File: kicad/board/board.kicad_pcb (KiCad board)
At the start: 2 copper layers, 126.9 x 103.7 mm, 43 parts

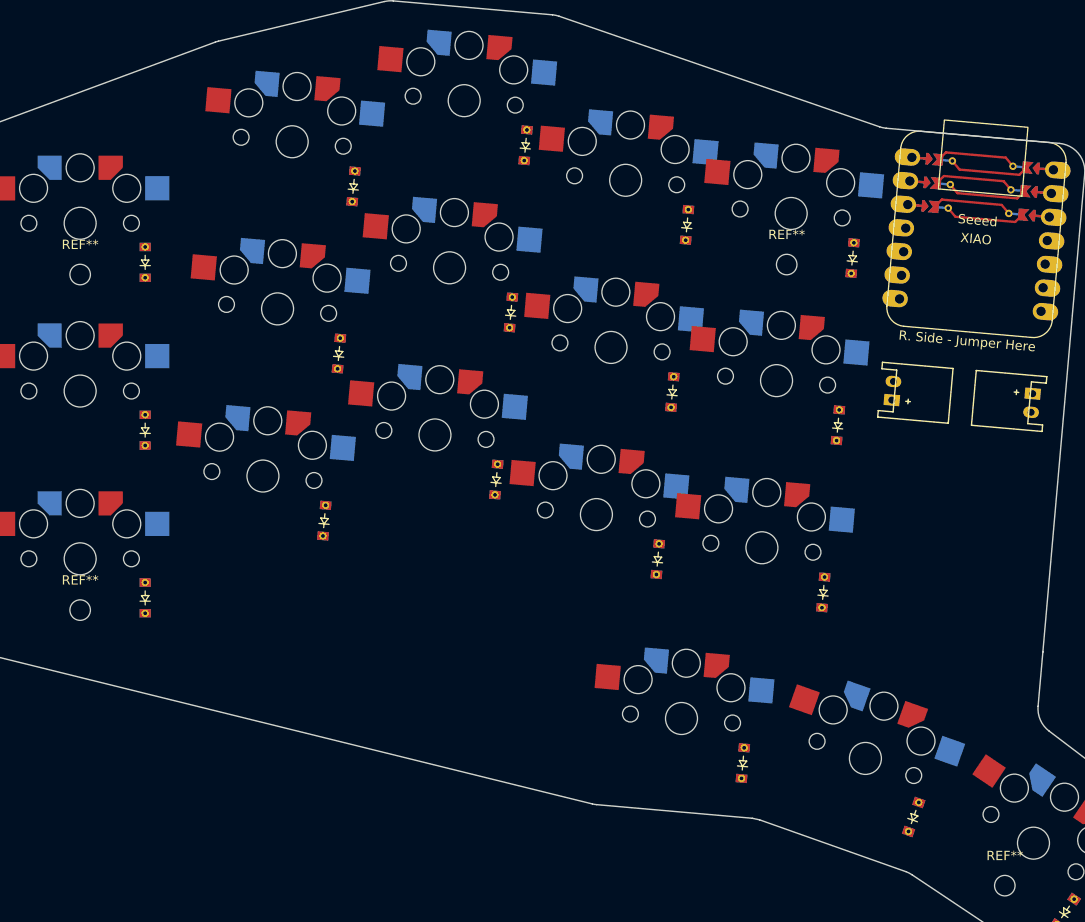
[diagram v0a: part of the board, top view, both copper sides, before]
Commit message: added diodes
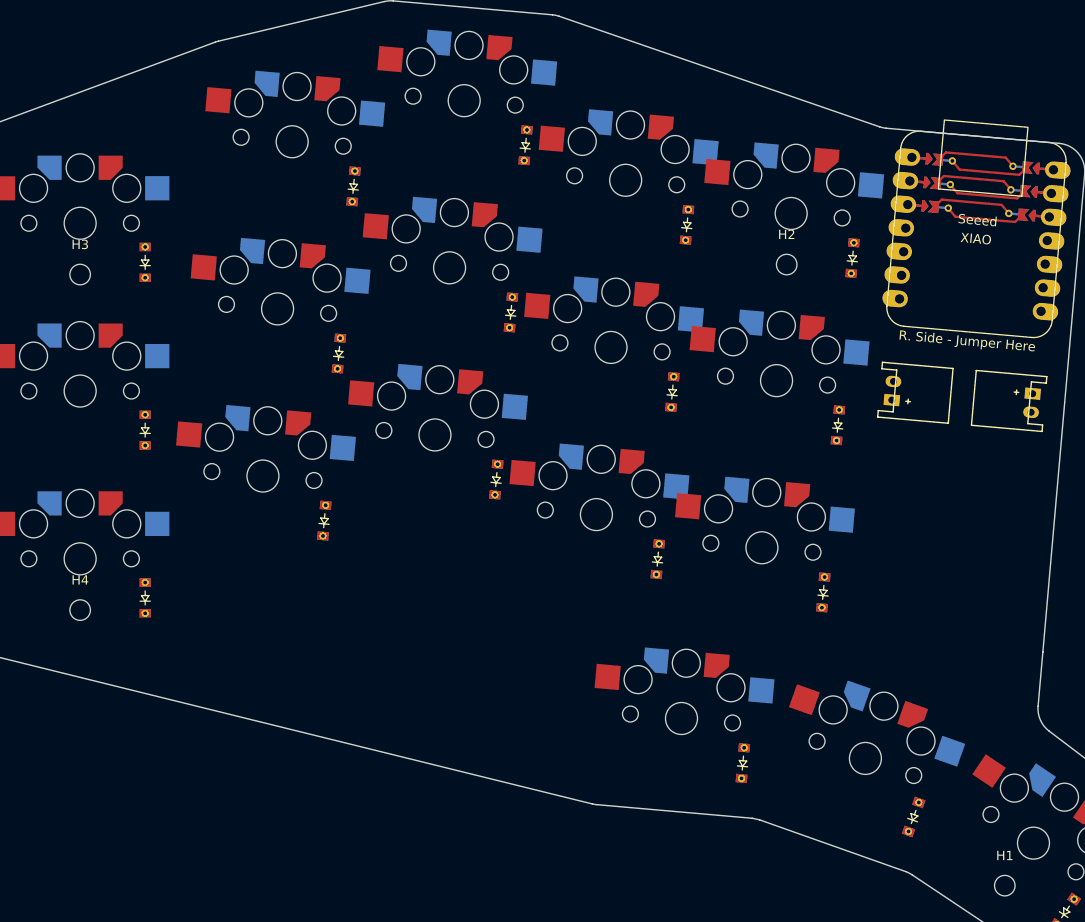
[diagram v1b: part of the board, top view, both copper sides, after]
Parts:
- renumbered REF** to H1, REF** to H2, REF** to H3, REF** to H4
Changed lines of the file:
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@@
 		)
 		(pad "" np_thru_hole circle
-			(at 5.000001 -3.75 355)
+			(at 5.000002 -3.75 355)
 			(size 3 3)
 			(drill 3)
@@
 		)
 		(pad "" np_thru_hole circle
-			(at 5.000001 -3.75 355)
+			(at 5.000002 -3.75 355)
 			(size 3 3)
 			(drill 3)
@@
 		(descr "Mounting Hole 2.2mm, no annular, M2")
 		(tags "mounting hole 2.2mm no annular m2")
-		(property "Reference" "REF**"
+		(property "Reference" "H3"
 			(at 0 -3.2 0)
 			(layer "F.SilkS")
@@
 		)
 		(pad "" np_thru_hole circle
-			(at 5.000001 -3.75 355)
+			(at 5.000002 -3.75 355)
 			(size 3 3)
 			(drill 3)
@@
 		)
 		(pad "" np_thru_hole circle
-			(at 5.000001 -3.75 355)
+			(at 5.000002 -3.75 355)
 			(size 3 3)
 			(drill 3)
@@
 		)
 		(pad "" np_thru_hole circle
-			(at 5.000001 -3.75 355)
+			(at 5.000002 -3.75 355)
 			(size 3 3)
 			(drill 3)
@@
 		)
 		(pad "" np_thru_hole circle
-			(at 5.000001 -3.75 355)
+			(at 5.000002 -3.75 355)
 			(size 3 3)
 			(drill 3)
@@
 		(at 19.610296 -8.88183 -5)
 		(property "Reference" "S4"
-			(at 0 0 -5)
+			(at 0 0 175)
 			(layer "F.SilkS")
 			(hide yes)
@@
 		)
 		(property "Value" "SW_Push_45deg"
-			(at 0 0 -5)
+			(at 0 0 175)
 			(layer "F.SilkS")
 			(hide yes)
@@
 		)
 		(property "Footprint" ""
-			(at 0 0 -5)
+			(at 0 0 175)
 			(layer "F.Fab")
 			(hide yes)
@@
 		)
 		(property "Datasheet" ""
-			(at 0 0 -5)
+			(at 0 0 175)
 			(layer "F.Fab")
 			(hide yes)
@@
 		)
 		(property "Description" "Push button switch, normally open, two pins, 45° tilted"
-			(at 0 0 -5)
+			(at 0 0 175)
 			(layer "F.Fab")
 			(hide yes)
@@
 		)
 		(pad "" np_thru_hole circle
-			(at 5.000001 -3.75 355)
+			(at 5.000002 -3.75 355)
 			(size 3 3)
 			(drill 3)
@@
 		)
 		(pad "" np_thru_hole circle
-			(at 5.000001 -3.75 355)
+			(at 5.000002 -3.75 355)
 			(size 3 3)
 			(drill 3)
@@
 		(descr "Mounting Hole 2.2mm, no annular, M2")
 		(tags "mounting hole 2.2mm no annular m2")
-		(property "Reference" "REF**"
+		(property "Reference" "H1"
 			(at 0 -3.2 0)
 			(layer "F.SilkS")
@@
 			(size 2.2 2.2)
 			(drill 2.2)
-			(layers "*.Cu" "*.Mask")
+			(layers "F&B.Cu" "*.Mask")
 		)
 	)
@@
 		)
 		(pad "" np_thru_hole circle
-			(at 5.000001 -3.75 355)
+			(at 5.000002 -3.75 355)
 			(size 3 3)
 			(drill 3)
@@
 		)
 		(property "Footprint" ""
-			(at 0 0 -5)
+			(at 0 0 175)
 			(layer "F.Fab")
 			(hide yes)
@@
 		)
 		(property "Datasheet" ""
-			(at 0 0 -5)
+			(at 0 0 175)
 			(layer "F.Fab")
 			(hide yes)
@@
 		)
 		(property "Description" ""
-			(at 0 0 -5)
+			(at 0 0 175)
 			(layer "F.Fab")
 			(hide yes)
@@
 		)
 		(pad "1" smd custom
-			(at -4.775001 -5.08 355)
+			(at -4.775002 -5.08 355)
 			(size 0.2 0.2)
 			(layers "B.Cu" "B.Mask")
@@
 		)
 		(pad "2" thru_hole circle
-			(at -3.262001 -2.54)
+			(at -3.262002 -2.54)
 			(size 0.8 0.8)
 			(drill 0.4)
@@
 		)
 		(pad "12" smd custom
-			(at -4.775001 -5.08 355)
+			(at -4.775002 -5.08 355)
 			(size 0.2 0.2)
 			(layers "F.Cu" "F.Mask")
@@
 		(descr "Mounting Hole 2.2mm, no annular, M2")
 		(tags "mounting hole 2.2mm no annular m2")
-		(property "Reference" "REF**"
+		(property "Reference" "H2"
 			(at 0 -3.2 0)
 			(layer "F.SilkS")
@@
 		)
 		(pad "" np_thru_hole circle
-			(at 5.000001 -3.75 355)
+			(at 5.000002 -3.75 355)
 			(size 3 3)
 			(drill 3)
@@
 		(descr "Mounting Hole 2.2mm, no annular, M2")
 		(tags "mounting hole 2.2mm no annular m2")
-		(property "Reference" "REF**"
+		(property "Reference" "H4"
 			(at 0 -3.2 0)
 			(layer "F.SilkS")
@@
 		)
 		(pad "" np_thru_hole circle
-			(at 5.000001 -3.75 355)
+			(at 5.000002 -3.75 355)
 			(size 3 3)
 			(drill 3)
@@
 		)
 		(pad "" np_thru_hole circle
-			(at 5.000001 -3.75 355)
+			(at 5.000002 -3.75 355)
 			(size 3 3)
 			(drill 3)
@@
 		)
 		(pad "" np_thru_hole circle
-			(at 5.000001 -3.75 355)
+			(at 5.000002 -3.75 355)
 			(size 3 3)
 			(drill 3)

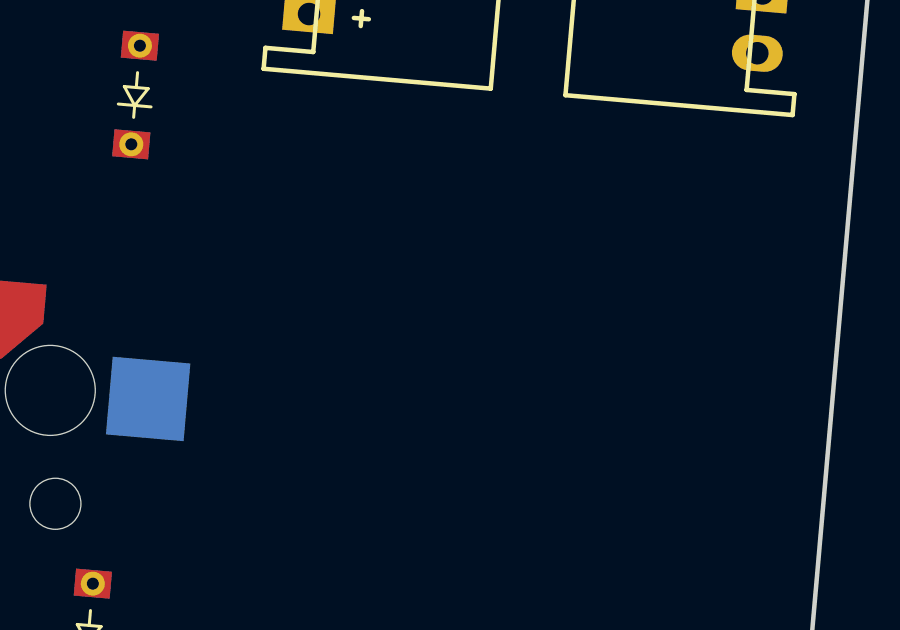
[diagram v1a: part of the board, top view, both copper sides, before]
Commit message: fixed footprints
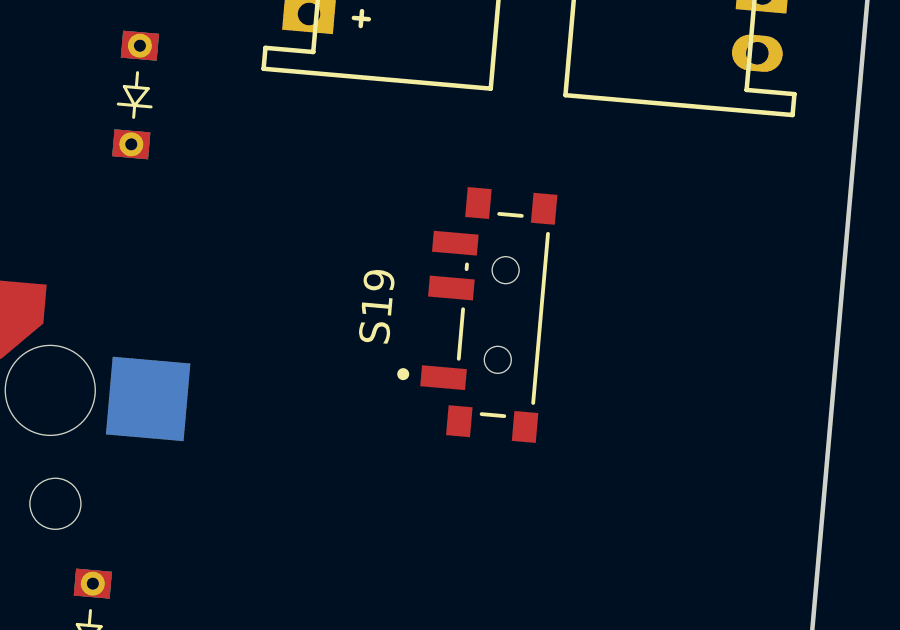
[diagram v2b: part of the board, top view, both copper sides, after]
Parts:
- added S19: SW_SSSS811101, sCLACKEN:SW_SSSS811101, F.Cu at (93.5, -7.00)

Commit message: we messed up pcb
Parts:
- added S20: SSSS811101, sCLACKEN:SW_SSSS811101, B.Cu at (255.0, 154.5)
- D1, D10, D11, D12, D13, D14, D15, D16, D17, D18, D2, D3, D4, D5, D6, D7, D8, D9: value 1N914 -> D
- H1, H2, H3, H4: value MountingHole_2.2mm_M2 -> MountingHole
- S1, S10, S11, S12, S13, S14, S15, S16, S17, S18, S2, S3, S4, S5, S6, S7, S8, S9: value SW_Push_45deg -> SW_SPST
- S19: value SW_SSSS811101 -> SSSS811101
- U1: value (none) -> ~; footprint xiao-ble-tht -> clacken:seeed_xaio
- moved S19 228.4 mm to (255.0, 154.5)
- moved D11 220.4 mm to (216.0, 141.2)
- moved D12 220.4 mm to (217.6, 123.3)
- moved D14 220.4 mm to (233.8, 144.8)
- moved D15 220.4 mm to (235.3, 126.9)
- moved D18 220.4 mm to (258.2, 197.0)
- moved D3 220.4 mm to (159.4, 127.3)
- moved D7 220.4 mm to (197.1, 150.6)
- moved D9 220.4 mm to (200.2, 114.8)
- moved H2 220.4 mm to (228.3, 127.6)
- moved H3 220.4 mm to (152.5, 128.6)
- moved H4 220.4 mm to (152.5, 164.6)
- moved JST1 220.4 mm to (239.6, 141.1)
- moved JST2 220.4 mm to (254.6, 142.4)
- moved S1 220.4 mm to (152.5, 159.1)
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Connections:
- D1 pad 1: Row3 -> G2
- D10 pad 1: Row3 -> G2
- D11 pad 1: Row2 -> G1
- D12 pad 1: Row1 -> G0
- D13 pad 1: Row3 -> G2
- D14 pad 1: Row2 -> G1
- D15 pad 1: Row1 -> G0
- D16 pad 1: Row4 -> G3
- D17 pad 1: Row4 -> G3
- D18 pad 1: Row4 -> G3
- D2 pad 1: Row2 -> G1
- D3 pad 1: Row1 -> G0
- D4 pad 1: Row3 -> G2
- D5 pad 1: Row2 -> G1
- D6 pad 1: Row1 -> G0
- D7 pad 1: Row3 -> G2
- D8 pad 1: Row2 -> G1
- D9 pad 1: Row1 -> G0
- JST2 pad 1: Net-(JST1-Pin_1) -> Net-(JST1-Pin_2)
- JST2 pad 2: Net-(JST1-Pin_2) -> Net-(JST2-Pin_2)
- S1 pad 1: Col1 -> Net-(D1-A)
- S1 pad 2: Net-(D1-A) -> C0
- S10 pad 1: Col4 -> Net-(D10-A)
- S10 pad 2: Net-(D10-A) -> C3
- S11 pad 1: Col4 -> Net-(D11-A)
- S11 pad 2: Net-(D11-A) -> C3
- S12 pad 1: Col4 -> Net-(D12-A)
- S12 pad 2: Net-(D12-A) -> C3
- S13 pad 1: Col5 -> Net-(D13-A)
- S13 pad 2: Net-(D13-A) -> C4
- S14 pad 1: Col5 -> Net-(D14-A)
- S14 pad 2: Net-(D14-A) -> C4
- S15 pad 1: Col5 -> Net-(D15-A)
- S15 pad 2: Net-(D15-A) -> C4
- S16 pad 1: Col3 -> Net-(D16-A)
- S16 pad 2: Net-(D16-A) -> C2
- S17 pad 1: Col4 -> Net-(D17-A)
- S17 pad 2: Net-(D17-A) -> C3
- S18 pad 1: Col5 -> Net-(D18-A)
- S18 pad 2: Net-(D18-A) -> C4
- S19 pad 1: (no net) -> unconnected-(S19-Pad1)
- S19 pad 2: (no net) -> Net-(JST1-Pin_1)
- S19 pad 3: (no net) -> Net-(JST2-Pin_2)
- S2 pad 1: Col1 -> Net-(D2-A)
- S2 pad 2: Net-(D2-A) -> C0
- S3 pad 1: Col1 -> Net-(D3-A)
- S3 pad 2: Net-(D3-A) -> C0
- S4 pad 1: Col2 -> Net-(D4-A)
- S4 pad 2: Net-(D4-A) -> C1
- S5 pad 1: Col2 -> Net-(D5-A)
- S5 pad 2: Net-(D5-A) -> C1
- S6 pad 1: Col2 -> Net-(D6-A)
- S6 pad 2: Net-(D6-A) -> C1
- S7 pad 1: Col3 -> Net-(D7-A)
- S7 pad 2: Net-(D7-A) -> C2
- S8 pad 1: Col3 -> Net-(D8-A)
- S8 pad 2: Net-(D8-A) -> C2
- S9 pad 1: Col3 -> Net-(D9-A)
- S9 pad 2: Net-(D9-A) -> C2
- U1 pad 0: P0 -> unconnected-(U1-P0-Pad0)_2
- U1 pad 1: P1 -> unconnected-(U1-P1-Pad1)_2
- U1 pad 10: P10 -> G0
- U1 pad 11: _1_11 -> unconnected-(U1-V3-Pad11)_1
- U1 pad 12: _1_12 -> unconnected-(U1-GND-Pad12)_1
- U1 pad 13: _1_13 -> unconnected-(U1-VCC-Pad13)
- U1 pad 2: P2 -> C0
- U1 pad 3: P3 -> C1
- U1 pad 4: P4 -> C2
- U1 pad 5: P5 -> C3
- U1 pad 6: P6 -> C4
- U1 pad 7: P7 -> G3
- U1 pad 8: P8 -> G2
- U1 pad 9: P9 -> G1
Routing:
- net C0: track 0.00 -> 214.5 mm, vias 0 -> 3
- net C2: track 0.00 -> 201.0 mm, vias 0 -> 4
- net C3: track 0.00 -> 186.1 mm, vias 0 -> 7
- net C1: track 0.00 -> 165.6 mm, vias 0 -> 3
- net C4: track 0.00 -> 155.1 mm, vias 0 -> 6
- net G3: track 0.00 -> 123.5 mm
- net G0: track 0.00 -> 122.3 mm
- net G1: track 0.00 -> 120.6 mm
- net G2: track 0.00 -> 100.1 mm
- net (no net): track 0.00 -> 99.6 mm
- net Net-(JST1-Pin_1): track 0.00 -> 28.5 mm, vias 0 -> 1
- net Net-(JST1-Pin_2): track 0.00 -> 15.5 mm
- net Net-(JST2-Pin_2): track 0.00 -> 10.3 mm
- net VCC: track 10.3 -> 0.00 mm
- net P0: track 10.3 -> 0.00 mm
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
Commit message: traces
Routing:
- net G2: track 100.1 -> 127.0 mm
- net (no net): track 99.6 -> 75.5 mm
- net Net-(D18-A): track 0.00 -> 21.3 mm, vias 0 -> 1
- net Net-(D16-A): track 0.00 -> 20.8 mm, vias 0 -> 1
- net Net-(D11-A): track 0.00 -> 19.6 mm, vias 0 -> 1
- net Net-(D2-A): track 0.00 -> 19.6 mm, vias 0 -> 1
- net Net-(D1-A): track 0.00 -> 19.6 mm, vias 0 -> 1
- net Net-(D10-A): track 0.00 -> 19.6 mm, vias 0 -> 1
- net Net-(D6-A): track 0.00 -> 19.5 mm, vias 0 -> 1
- net Net-(D15-A): track 0.00 -> 19.5 mm, vias 0 -> 1
- net Net-(D13-A): track 0.00 -> 19.4 mm, vias 0 -> 1
- net Net-(D17-A): track 0.00 -> 19.4 mm, vias 0 -> 1
- net Net-(D12-A): track 0.00 -> 19.3 mm, vias 0 -> 1
- net Net-(D3-A): track 0.00 -> 19.3 mm, vias 0 -> 1
- net Net-(D7-A): track 0.00 -> 19.3 mm, vias 0 -> 1
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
